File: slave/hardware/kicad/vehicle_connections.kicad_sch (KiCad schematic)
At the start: 2 parts, among them J2 AMPSEAL_8, J3 AMPSEAL_23

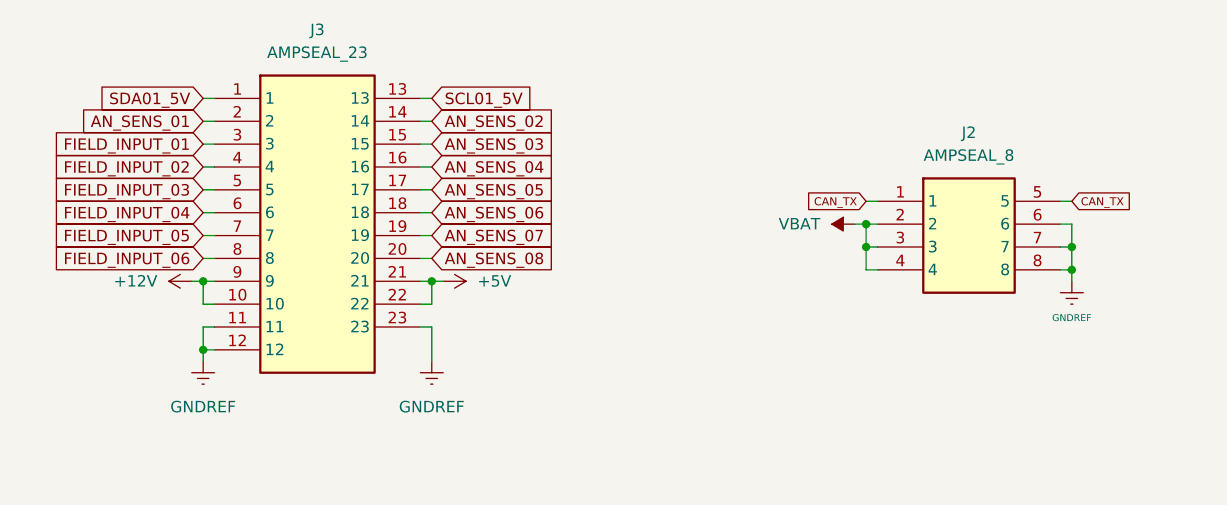
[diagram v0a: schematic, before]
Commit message: feat(HW): add MCU connections
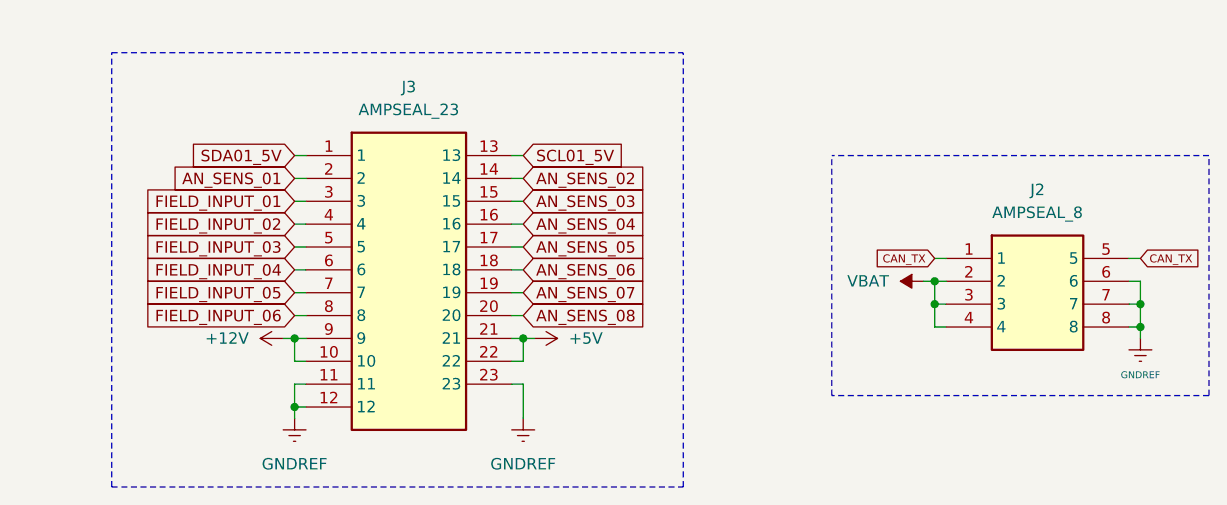
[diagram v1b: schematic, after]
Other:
- moved on the sheet: J2, J3

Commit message: feat(HW): finalize schematic design
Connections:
- net CAN_TX renamed CAN_H
- net CAN_H: no longer J2.5
- new net CAN_L: J2.5
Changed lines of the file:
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@@
-		)
-	)
-	(global_label "SDA01_5V"
-		(shape input)
-		(at 115.57 90.17 180)
-		(fields_autoplaced yes)
-		(effects
-			(font
-				(size 1.27 1.27)
-				(thickness 0.1111)
-			)
-			(justify right)
-		)
-		(property "Intersheetrefs" "${INTERSHEET_REFS}"
-			(at 103.5705 90.17 0)
-			(hide yes)
-			(show_name no)
-			(do_not_autoplace no)
-			(effects
-				(font
-					(size 1.27 1.27)
-				)
-				(justify right)
-			)
 		)
 	)
@@
 		)
 	)
-	(global_label "AN_SENS_07"
-		(shape input)
-		(at 140.97 105.41 0)
-		(fields_autoplaced yes)
-		(effects
-			(font
-				(size 1.27 1.27)
-			)
-			(justify left)
-		)
-		(property "Intersheetrefs" "${INTERSHEET_REFS}"
-			(at 155.627 105.41 0)
-			(hide yes)
-			(show_name no)
-			(do_not_autoplace no)
-			(effects
-				(font
-					(size 1.27 1.27)
-				)
-				(justify left)
-			)
-		)
-	)
-	(global_label "AN_SENS_02"
-		(shape input)
-		(at 140.97 92.71 0)
-		(fields_autoplaced yes)
-		(effects
-			(font
-				(size 1.27 1.27)
-			)
-			(justify left)
-		)
-		(property "Intersheetrefs" "${INTERSHEET_REFS}"
-			(at 155.627 92.71 0)
-			(hide yes)
-			(show_name no)
-			(do_not_autoplace no)
-			(effects
-				(font
-					(size 1.27 1.27)
-				)
-				(justify left)
-			)
-		)
-	)
-	(global_label "FIELD_INPUT_05"
-		(shape input)
-		(at 115.57 105.41 180)
-		(fields_autoplaced yes)
-		(effects
-			(font
-				(size 1.27 1.27)
-			)
-			(justify right)
-		)
-		(property "Intersheetrefs" "${INTERSHEET_REFS}"
-			(at 97.5867 105.41 0)
-			(hide yes)
-			(show_name no)
-			(do_not_autoplace no)
-			(effects
-				(font
-					(size 1.27 1.27)
-				)
-				(justify right)
-			)
-		)
-	)
-	(global_label "FIELD_INPUT_03"
-		(shape input)
-		(at 115.57 100.33 180)
-		(fields_autoplaced yes)
-		(effects
-			(font
-				(size 1.27 1.27)
-			)
-			(justify right)
-		)
-		(property "Intersheetrefs" "${INTERSHEET_REFS}"
-			(at 97.5867 100.33 0)
-			(hide yes)
-			(show_name no)
-			(do_not_autoplace no)
-			(effects
-				(font
-					(size 1.27 1.27)
-				)
-				(justify right)
-			)
-		)
-	)
-	(global_label "SCL01_5V"
-		(shape input)
-		(at 140.97 90.17 0)
-		(fields_autoplaced yes)
-		(effects
-			(font
-				(size 1.27 1.27)
-				(thickness 0.1111)
-			)
-			(justify left)
-		)
-		(property "Intersheetrefs" "${INTERSHEET_REFS}"
-			(at 152.909 90.17 0)
-			(hide yes)
-			(show_name no)
-			(do_not_autoplace no)
-			(effects
-				(font
-					(size 1.27 1.27)
-				)
-				(justify left)
-			)
-		)
-	)
-	(global_label "CAN_TX"
-		(shape input)
-		(at 209.55 101.6 0)
+	(global_label "CAN_H"
+		(shape input)
+		(at 186.69 101.6 180)
 		(fields_autoplaced yes)
 		(effects
@@
 				(thickness 0.1111)
 			)
-			(justify left)
-		)
-		(property "Intersheetrefs" "${INTERSHEET_REFS}"
-			(at 216.4231 101.6 0)
-			(hide yes)
-			(show_name no)
-			(do_not_autoplace no)
-			(effects
-				(font
-					(size 1.27 1.27)
-				)
-				(justify left)
+			(justify right)
+		)
+		(property "Intersheetrefs" "${INTERSHEET_REFS}"
+			(at 180.4096 101.6 0)
+			(hide yes)
+			(show_name no)
+			(do_not_autoplace no)
+			(effects
+				(font
+					(size 1.27 1.27)
+				)
+				(justify right)
+			)
+		)
+	)
+	(global_label "AN_SENS_07"
+		(shape input)
+		(at 140.97 105.41 0)
+		(fields_autoplaced yes)
+		(effects
+			(font
+				(size 1.27 1.27)
+			)
+			(justify left)
+		)
+		(property "Intersheetrefs" "${INTERSHEET_REFS}"
+			(at 155.627 105.41 0)
+			(hide yes)
+			(show_name no)
+			(do_not_autoplace no)
+			(effects
+				(font
+					(size 1.27 1.27)
+				)
+				(justify left)
+			)
+		)
+	)
+	(global_label "AN_SENS_02"
+		(shape input)
+		(at 140.97 92.71 0)
+		(fields_autoplaced yes)
+		(effects
+			(font
+				(size 1.27 1.27)
+			)
+			(justify left)
+		)
+		(property "Intersheetrefs" "${INTERSHEET_REFS}"
+			(at 155.627 92.71 0)
+			(hide yes)
+			(show_name no)
+			(do_not_autoplace no)
+			(effects
+				(font
+					(size 1.27 1.27)
+				)
+				(justify left)
+			)
+		)
+	)
+	(global_label "FIELD_INPUT_05"
+		(shape input)
+		(at 115.57 105.41 180)
+		(fields_autoplaced yes)
+		(effects
+			(font
+				(size 1.27 1.27)
+			)
+			(justify right)
+		)
+		(property "Intersheetrefs" "${INTERSHEET_REFS}"
+			(at 97.5867 105.41 0)
+			(hide yes)
+			(show_name no)
+			(do_not_autoplace no)
+			(effects
+				(font
+					(size 1.27 1.27)
+				)
+				(justify right)
+			)
+		)
+	)
+	(global_label "FIELD_INPUT_03"
+		(shape input)
+		(at 115.57 100.33 180)
+		(fields_autoplaced yes)
+		(effects
+			(font
+				(size 1.27 1.27)
+			)
+			(justify right)
+		)
+		(property "Intersheetrefs" "${INTERSHEET_REFS}"
+			(at 97.5867 100.33 0)
+			(hide yes)
+			(show_name no)
+			(do_not_autoplace no)
+			(effects
+				(font
+					(size 1.27 1.27)
+				)
+				(justify right)
+			)
+		)
+	)
+	(global_label "SCL01_5V"
+		(shape input)
+		(at 140.97 90.17 0)
+		(fields_autoplaced yes)
+		(effects
+			(font
+				(size 1.27 1.27)
+			)
+			(justify left)
+		)
+		(property "Intersheetrefs" "${INTERSHEET_REFS}"
+			(at 153.1475 90.17 0)
+			(hide yes)
+			(show_name no)
+			(do_not_autoplace no)
+			(effects
+				(font
+					(size 1.27 1.27)
+				)
+				(justify left)
+			)
+		)
+	)
+	(global_label "SDA01_5V"
+		(shape input)
+		(at 115.57 90.17 180)
+		(fields_autoplaced yes)
+		(effects
+			(font
+				(size 1.27 1.27)
+			)
+			(justify right)
+		)
+		(property "Intersheetrefs" "${INTERSHEET_REFS}"
+			(at 103.332 90.17 0)
+			(hide yes)
+			(show_name no)
+			(do_not_autoplace no)
+			(effects
+				(font
+					(size 1.27 1.27)
+				)
+				(justify right)
 			)
 		)
@@
 		)
 	)
-	(global_label "CAN_TX"
-		(shape input)
-		(at 186.69 101.6 180)
+	(global_label "CAN_L"
+		(shape input)
+		(at 209.55 101.6 0)
 		(fields_autoplaced yes)
 		(effects
@@
 				(thickness 0.1111)
 			)
-			(justify right)
-		)
-		(property "Intersheetrefs" "${INTERSHEET_REFS}"
-			(at 179.8169 101.6 0)
-			(hide yes)
-			(show_name no)
-			(do_not_autoplace no)
-			(effects
-				(font
-					(size 1.27 1.27)
-				)
-				(justify right)
-			)
-		)
+			(justify left)
+		)
+		(property "Intersheetrefs" "${INTERSHEET_REFS}"
+			(at 215.6188 101.6 0)
+			(hide yes)
+			(show_name no)
+			(do_not_autoplace no)
+			(effects
+				(font
+					(size 1.27 1.27)
+				)
+				(justify left)
+			)
+		)

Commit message: fix(HW): resolve KiCad ERC warnings
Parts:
- J2: footprint 17762791 -> Datalogger:17762791
- J3: footprint 24890081 -> Datalogger:24890081
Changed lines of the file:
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@@
 			)
 		)
-		(property "Footprint" "17762791"
+		(property "Footprint" "Datalogger:17762791"
 			(at 204.47 196.52 0)
-			(hide yes)
 			(show_name no)
 			(do_not_autoplace no)
@@
 			)
 		)
-		(property "Footprint" "24890081"
+		(property "Footprint" "Datalogger:24890081"
 			(at 135.89 185.09 0)
-			(hide yes)
-			(show_name no)
-			(do_not_autoplace no)
+			(show_name no)
+			(do_not_autoplace no)

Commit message: feat(HW): begin PCB layout design
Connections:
- net +12V: now also J3.17, J3.18; no longer J3.10, J3.9
- net +5V: now also J3.19, J3.20; no longer J3.21, J3.22
- net AN_SENS_01: now also J3.1; no longer J3.2
- net AN_SENS_02: now also J3.2; no longer J3.14
- net AN_SENS_03: now also J3.3; no longer J3.15
- net AN_SENS_04: now also J3.4; no longer J3.16
- net AN_SENS_05: now also J3.5; no longer J3.17
- net AN_SENS_06: now also J3.6; no longer J3.18
- net AN_SENS_07: now also J3.7; no longer J3.19
- net AN_SENS_08: now also J3.8; no longer J3.20
- net FIELD_INPUT_01: now also J3.9; no longer J3.3
- net FIELD_INPUT_02: now also J3.10; no longer J3.4
- net FIELD_INPUT_03: now also J3.11; no longer J3.5
- net FIELD_INPUT_04: now also J3.12; no longer J3.6
- net FIELD_INPUT_05: now also J3.13; no longer J3.7
- net FIELD_INPUT_06: now also J3.16; no longer J3.8
- net GNDREF: now also J3.21, J3.22; no longer J3.11, J3.12
- net SCL01_5V: now also J3.14; no longer J3.13
- net SDA01_5V: now also J3.15; no longer J3.1

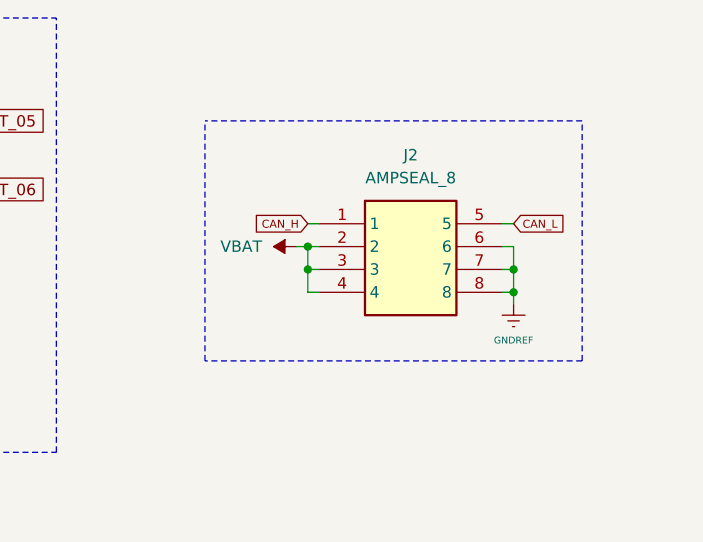
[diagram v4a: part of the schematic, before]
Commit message: feat(HW): continue PCB layout and routing updates
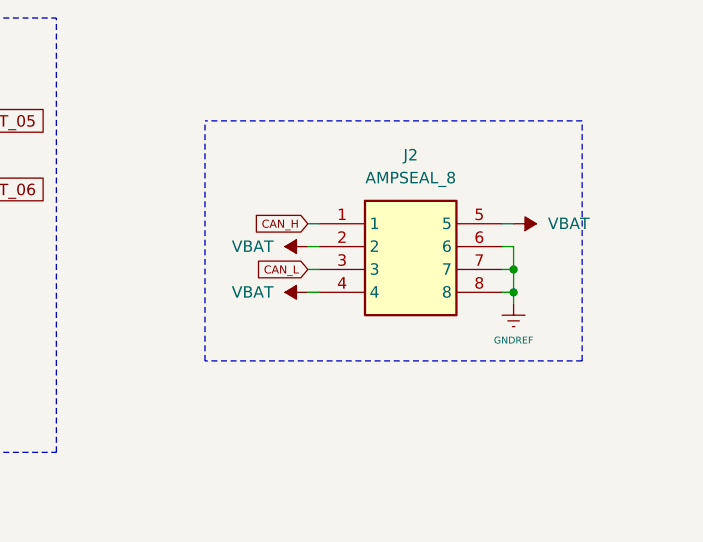
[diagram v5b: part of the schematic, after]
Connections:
- net CAN_L: now also J2.3; no longer J2.5
- net VBAT: now also J2.5; no longer J2.3
